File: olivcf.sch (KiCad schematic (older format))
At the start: 18 parts

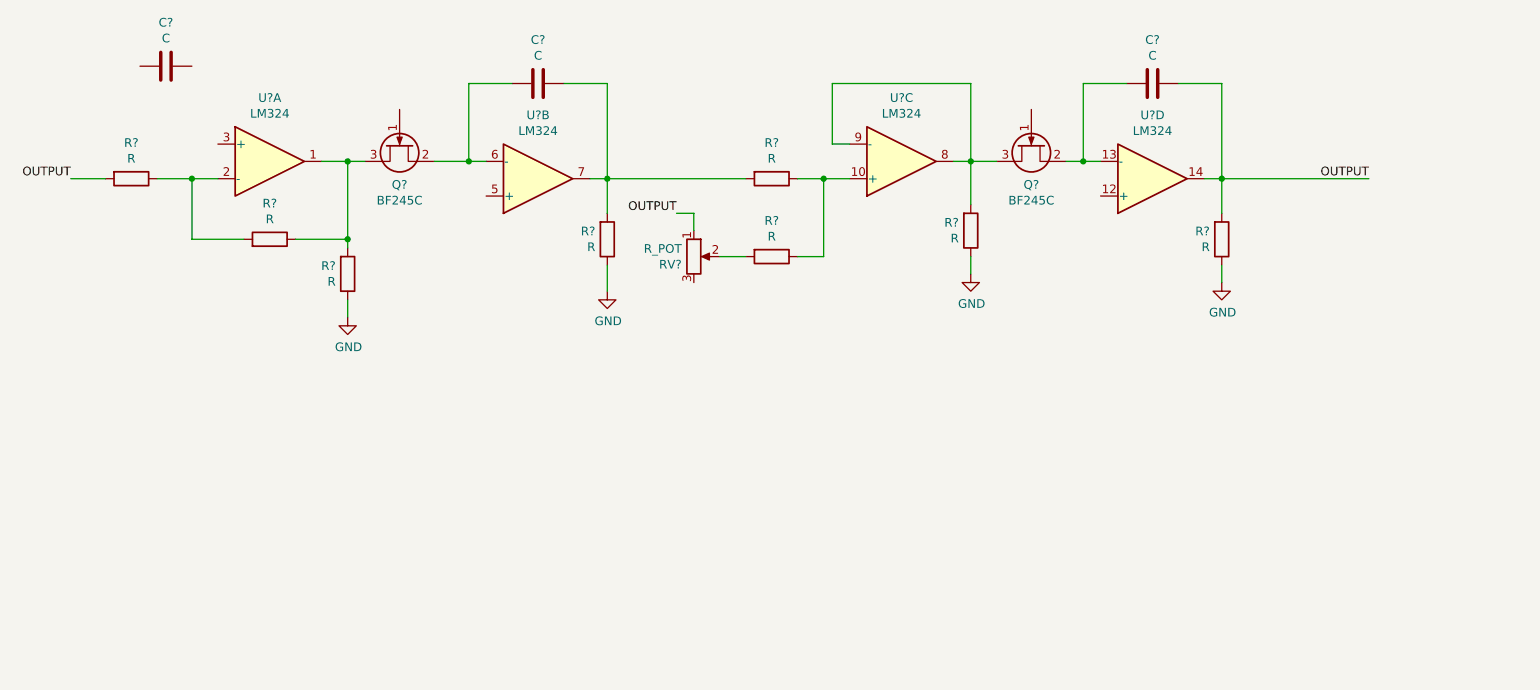
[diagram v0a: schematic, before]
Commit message: Main drawing added.
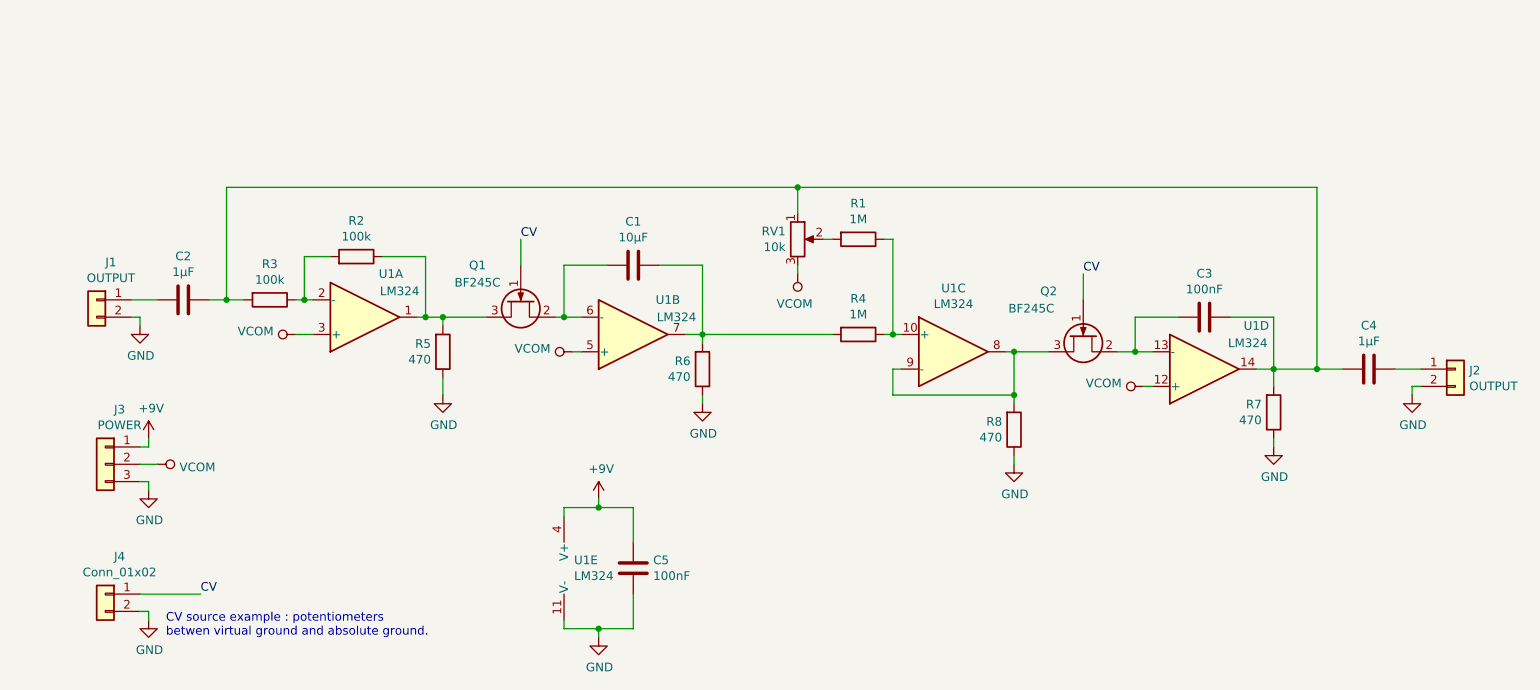
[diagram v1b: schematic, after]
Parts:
- added C2: 1µF, symbol Device:C
- added C5: 100nF, symbol Device:C
- added J1, J2: OUTPUT, symbol Connector_Generic:Conn_01x02
- added J3: POWER, symbol Connector_Generic:Conn_01x03
- added J4: Conn_01x02, symbol Connector_Generic:Conn_01x02
- added unit 5 of U1
- C1: renamed from C?; value C -> 10µF
- C3: renamed from C?; value C -> 100nF
- C4: renamed from C?; value C -> 1µF
- R1, R4: renamed from R?; value R -> 1M
- R2, R3: renamed from R?; value R -> 100k
- R5, R6, R7, R8: renamed from R?; value R -> 470
- RV1: renamed from RV?; value R_POT -> 10k
- gave numbers to parts that had none: 3
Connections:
- net OUTPUT is gone; now on an unnamed net: C3.1, R3.2, R7.2, RV1.1, U1.14
- net GND: now also C5.2, J1.2 (Pin_2), J2.2 (Pin_2), J3.3 (Pin_3), J4.2 (Pin_2), U1.11 (V-)
- net VCOM: now reaches U1.3 (+)
- net VCOM: now also RV1.3, U1.12 (+), U1.5 (+), J3.2 (Pin_2)
- net CV: now reaches Q1.1 (G)
- net CV: now also Q2.1 (G), J4.1 (Pin_1)
- net at C4.1: now also J2.1 (Pin_1)
- net at C4.2: now also C2.1
- new net: C2.2, J1.1 (Pin_1)
- new net +9V: C5.1, J3.1 (Pin_1), U1.4 (V+)
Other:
- note added: "CV source example : potentiometers\nbetwen virtual ground and absolute ground."
- moved on the sheet: C1, C3, C4, Q1, Q2, R1, R2, R3, R4, R5, R6, R7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
